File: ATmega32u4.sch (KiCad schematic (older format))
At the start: 27 parts, among them J1 USB_B_Mini, J2 AVR-ISP-6, U4 ATmega32U4RC-MU, Y1 16MHz

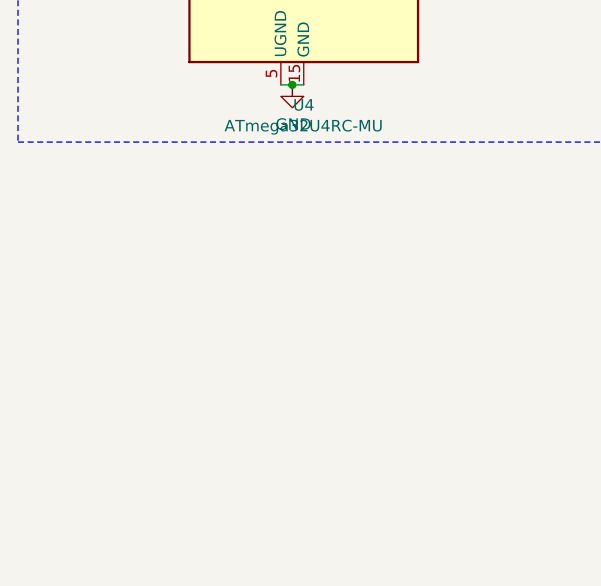
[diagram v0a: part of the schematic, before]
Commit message: Rename a global label to match event name
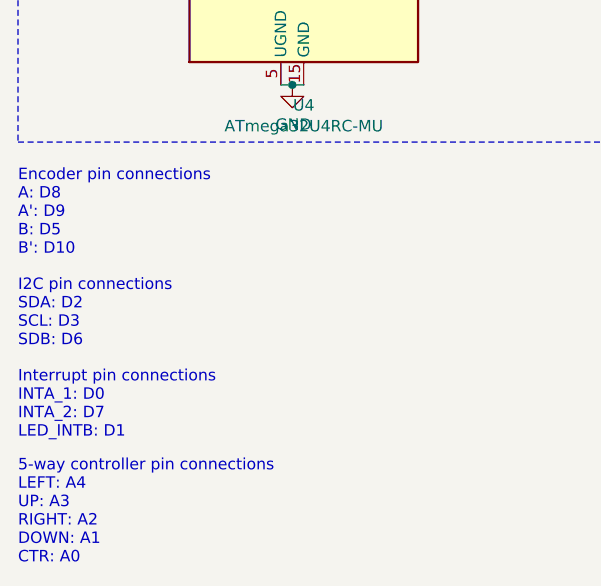
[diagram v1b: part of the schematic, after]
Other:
- note added: "5-way controller pin connections\nLEFT: A4\nUP: A3\nRIGHT: A2\nDOWN: A1\nCTR: A0"
- note added: "Encoder pin connections\nA: D8\nA': D9\nB: D5\nB': D10"
- note added: "I2C pin connections\nSDA: D2\nSCL: D3\nSDB: D6"
- note added: "Interrupt pin connections\nINTA_1: D0\nINTA_2: D7\nLED_INTB: D1"
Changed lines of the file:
@@
 Text HLabel 2400 4050 2    50   Input ~ 0
 LEFT
+Text Notes 550  5600 0    50   ~ 0
+Encoder pin connections\nA: D8\nA': D9\nB: D5\nB': D10
+Text Notes 550  6000 0    50   ~ 0
+I2C pin connections\nSDA: D2\nSCL: D3\nSDB: D6
+Text Notes 550  6400 0    50   ~ 0
+Interrupt pin connections\nINTA_1: D0\nINTA_2: D7\nLED_INTB: D1
+Text Notes 550  6950 0    50   ~ 0
+5-way controller pin connections\nLEFT: A4\nUP: A3\nRIGHT: A2\nDOWN: A1\nCTR: A0
 $EndSCHEMATC
